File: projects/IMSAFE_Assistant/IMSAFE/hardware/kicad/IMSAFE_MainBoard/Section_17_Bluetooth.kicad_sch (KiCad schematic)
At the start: 0 parts

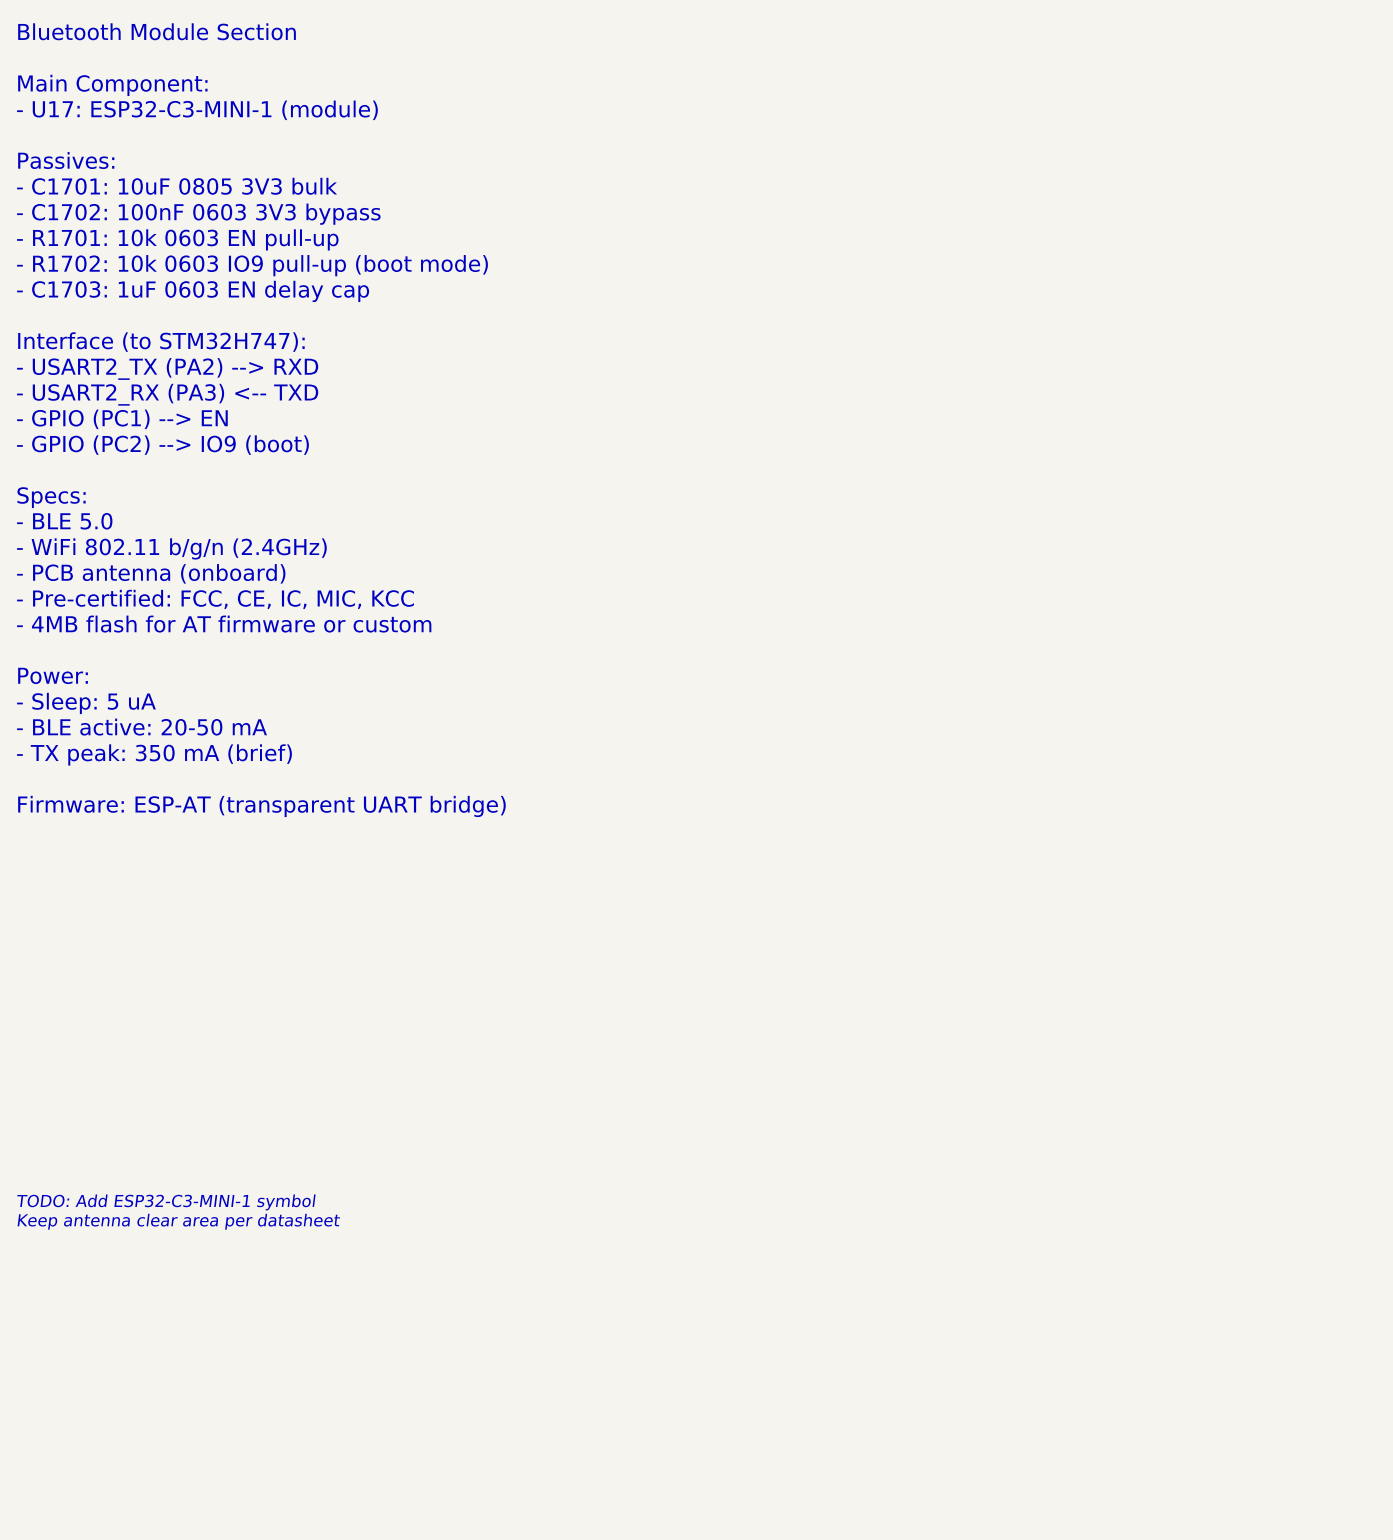
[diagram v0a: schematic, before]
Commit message: Update KiCad schematics and add analysis files
- Update all MainBoard schematic sections with component placement
- Add ERC reports and analysis scripts for schematic validation
- Update Radar Interface and SwitchLED Board projects
- Sync KiCad project files with latest session changes

Co-Authored-By: Claude Opus 4.5 <noreply@anthropic.com>
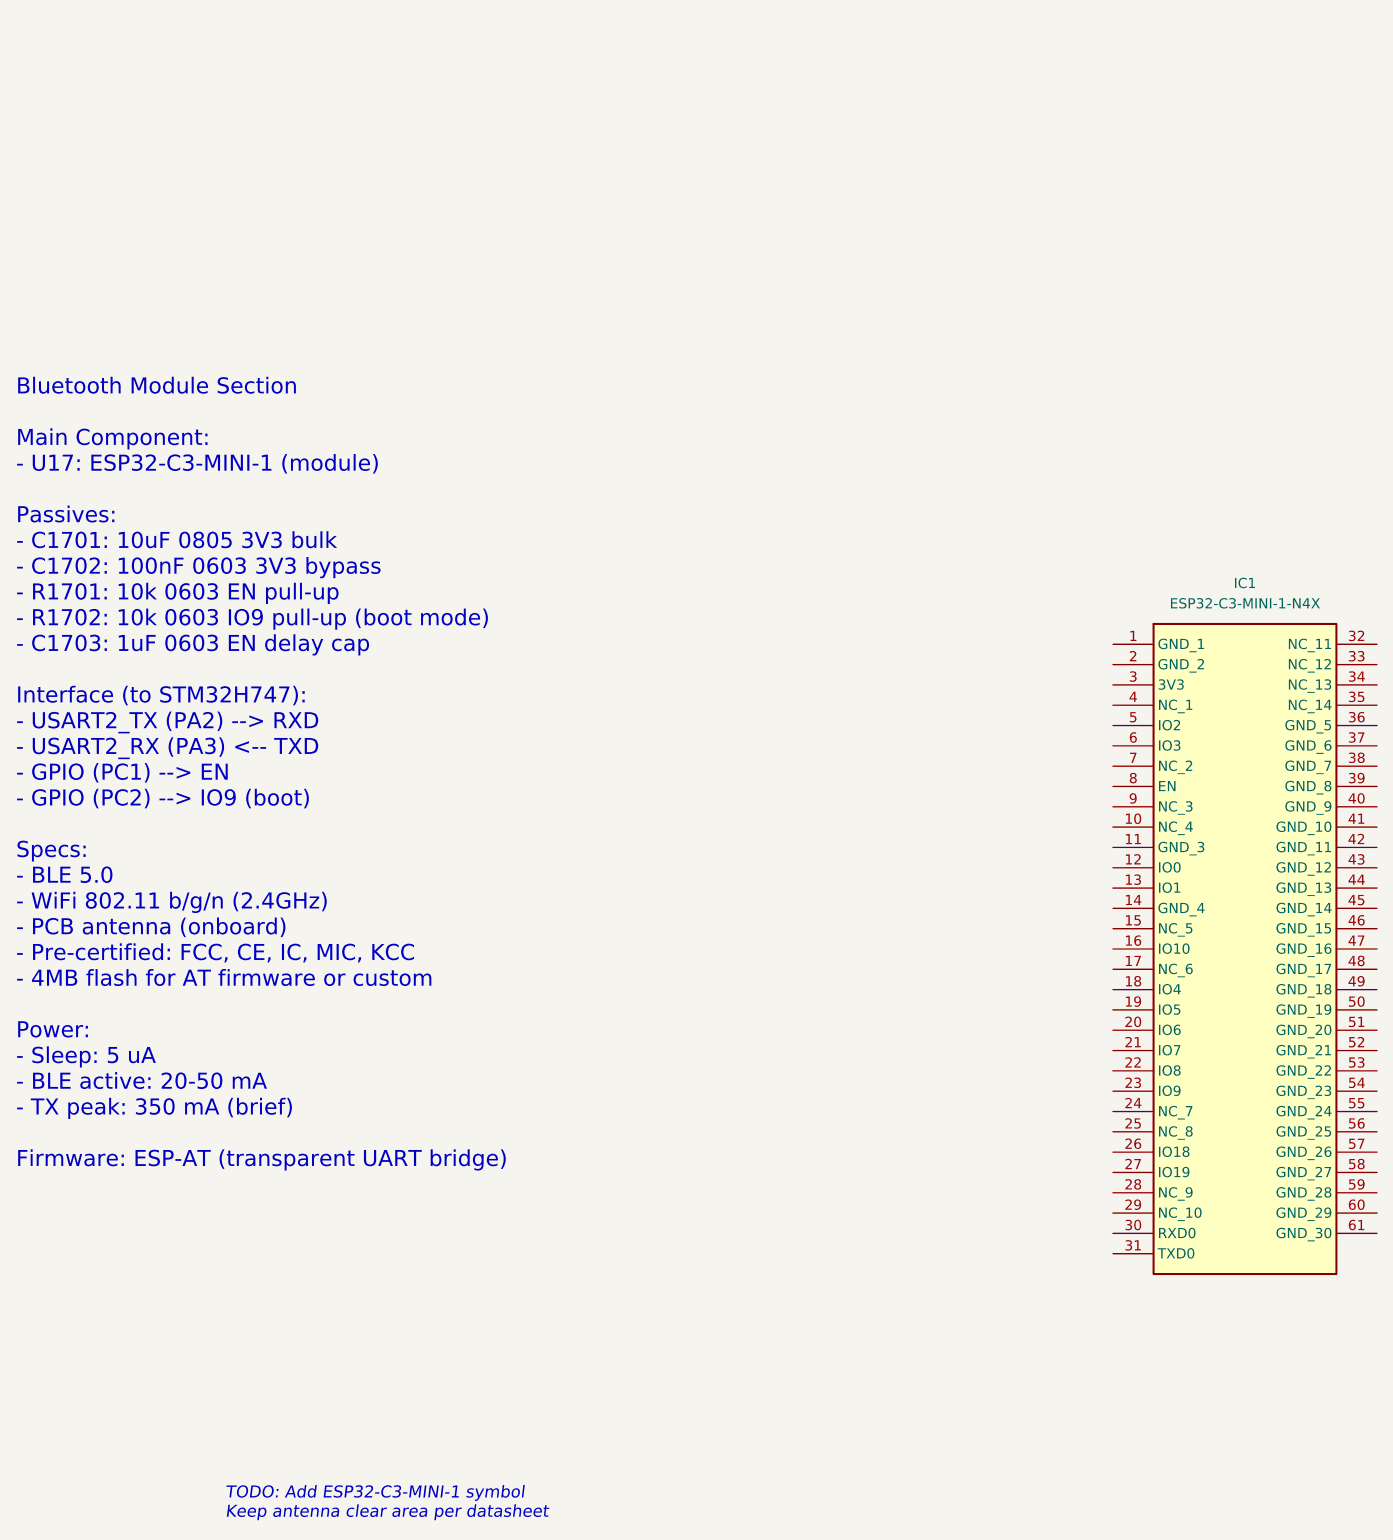
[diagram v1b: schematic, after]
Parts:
- added IC1: ESP32-C3-MINI-1-N4X, ESP32C3MINI1N4X, symbol 1_New_library:ESP32-C3-MINI-1-N4X
